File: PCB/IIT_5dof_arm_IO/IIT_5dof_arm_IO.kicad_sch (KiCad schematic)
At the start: 69 parts, among them J1 Conn_02x13_Top_Bottom, J10 Conn_01x06, J11 Conn_01x06, J12 Conn_01x04, J13 Conn_01x04, J2 Conn_01x06, J3 Conn_01x06, J4 Conn_01x06, J5 Conn_01x05, J6 Conn_01x03, J7 Conn_02x03_Counter_Clockwise, J8 Conn_01x03, J9 Conn_01x06, SW1 SW_Push, SW10 SW_Push, SW11 SW_Push, SW12 SW_Push, SW13 SW_Push, SW14 SW_Push, SW2 SW_Push, SW3 SW_Push, SW4 SW_Push, SW5 SW_Push, SW6 SW_Push, SW7 RotaryEncoder_Switch, SW8 SW_Push, SW9 SW_Push, U1 ATmega328P-A, Y1 16MHz

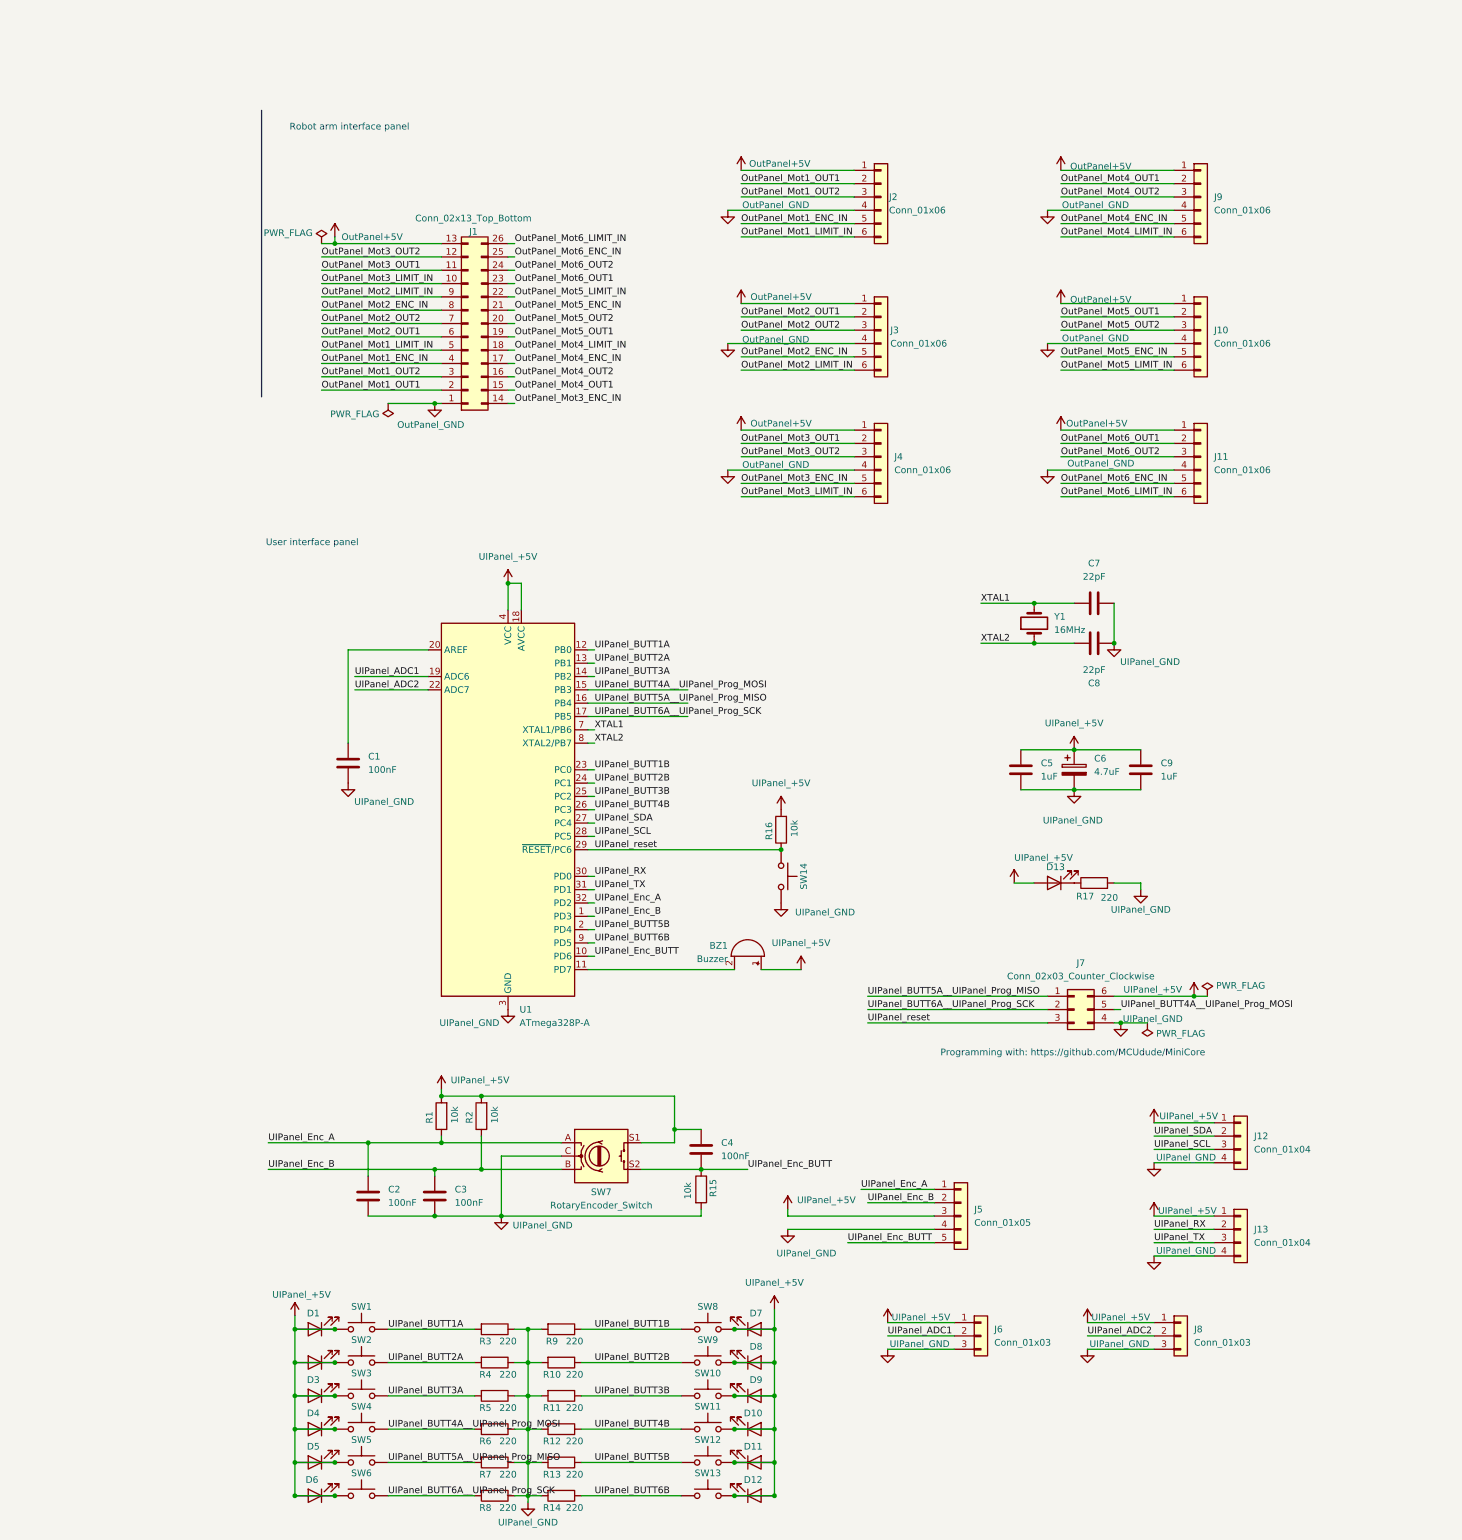
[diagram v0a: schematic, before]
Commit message: Split control board and I/O cards into separate projects
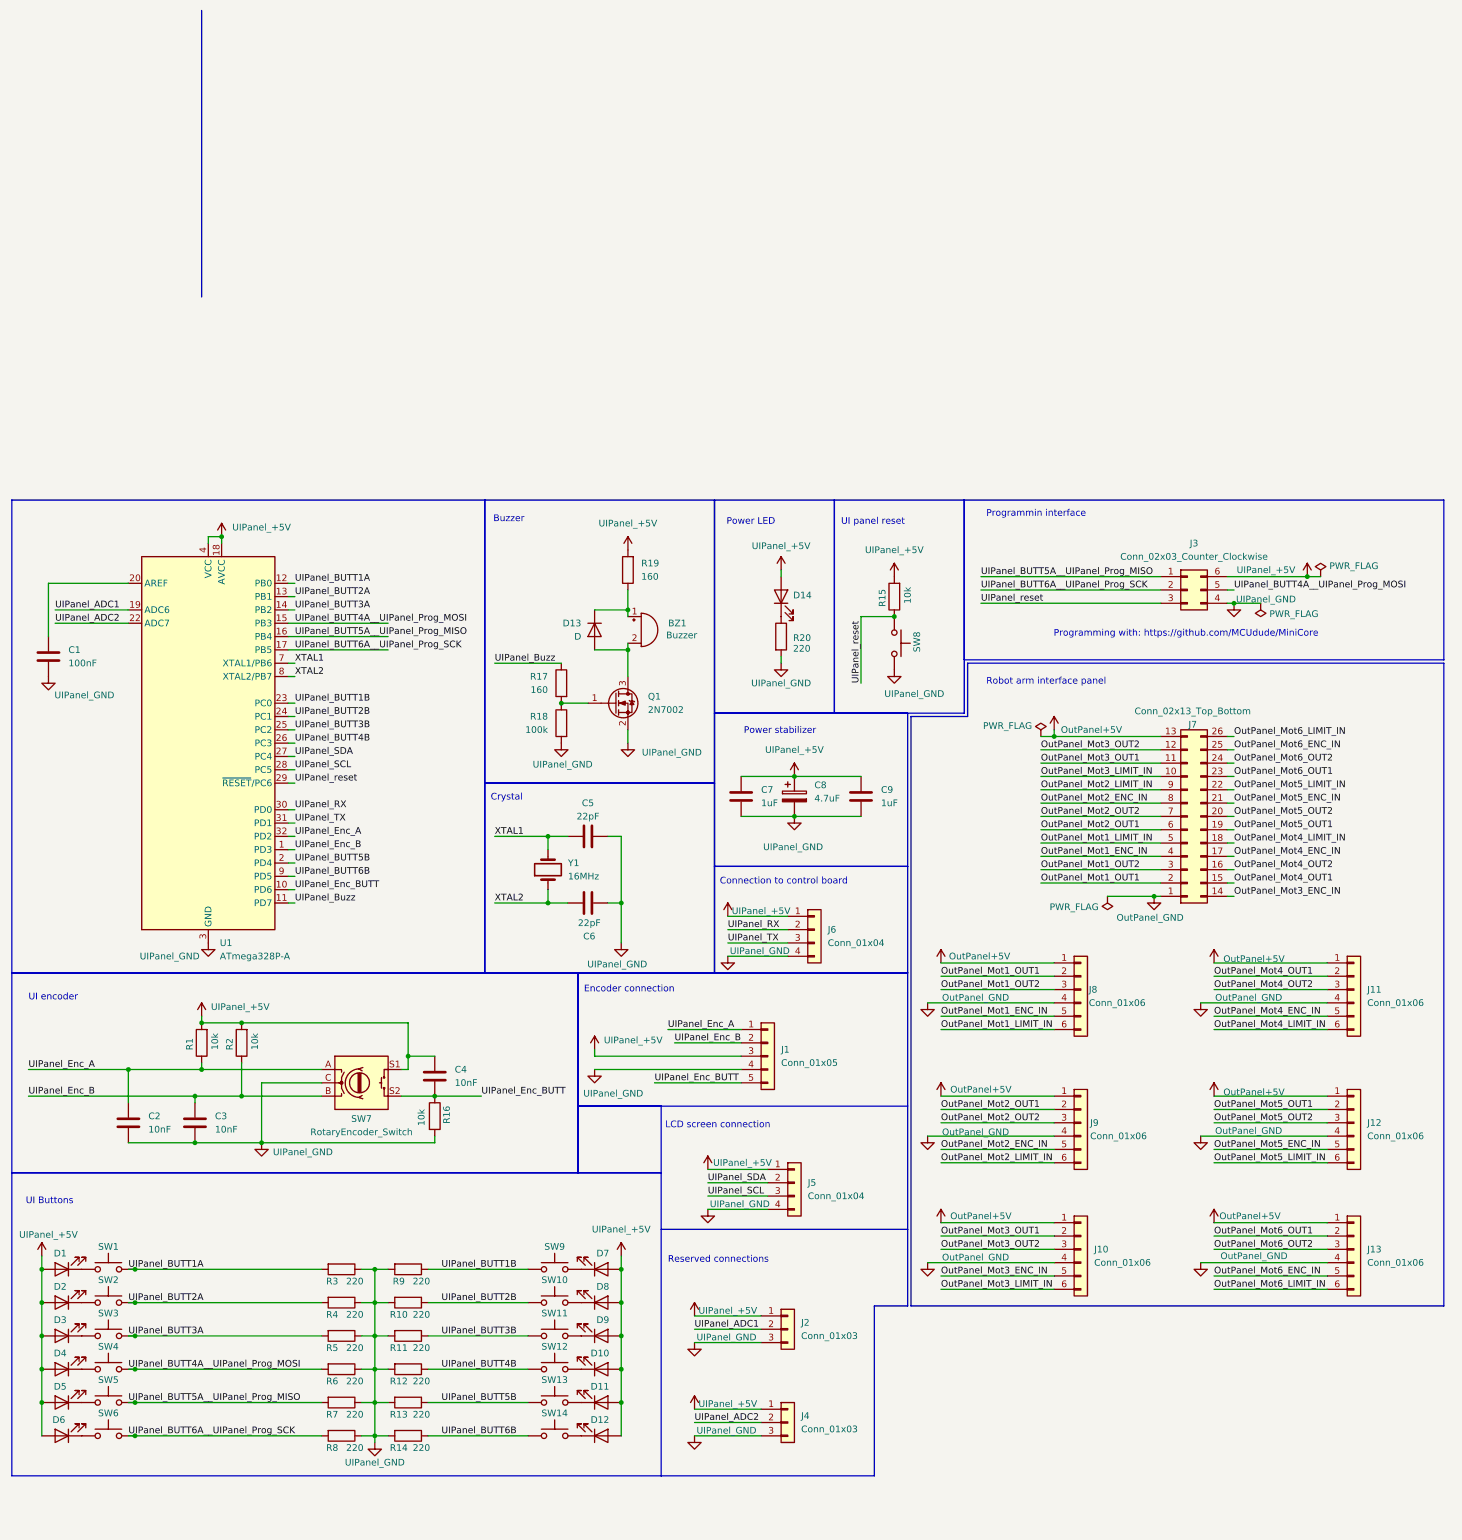
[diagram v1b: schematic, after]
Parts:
- removed C6: 4.7uF, Capacitor_SMD:C_1206_3216Metric_Pad1.33x1.80mm_HandSolder, symbol Device:C_Polarized
- removed C8: 22pF, Capacitor_SMD:C_0805_2012Metric_Pad1.18x1.45mm_HandSolder, symbol Device:C
- removed D13: LED, LED_THT:LED_D5.0mm, symbol Device:LED
- removed J1: Conn_02x13_Top_Bottom, Connector_IDC:IDC-Header_2x13_P2.54mm_Vertical, symbol Connector_Generic:Conn_02x13_Top_Bottom
- removed J12, J13: Conn_01x04, Connector_Molex:Molex_KK-254_AE-6410-04A_1x04_P2.54mm_Vertical, symbol Connector_Generic:Conn_01x04
- removed J2, J3, J4: Conn_01x06, Connector_Molex:Molex_KK-254_AE-6410-06A_1x06_P2.54mm_Vertical, symbol Connector_Generic:Conn_01x06
- removed J5: Conn_01x05, Connector_Molex:Molex_KK-254_AE-6410-05A_1x05_P2.54mm_Vertical, symbol Connector_Generic:Conn_01x05
- removed J6, J8: Conn_01x03, Connector_Molex:Molex_KK-254_AE-6410-03A_1x03_P2.54mm_Vertical, symbol Connector_Generic:Conn_01x03
- removed J7: Conn_02x03_Counter_Clockwise, Connector_PinHeader_2.54mm:PinHeader_2x03_P2.54mm_Vertical, symbol Connector_Generic:Conn_02x03_Counter_Clockwise
- added C6: 22pF, Capacitor_SMD:C_0805_2012Metric_Pad1.18x1.45mm_HandSolder, symbol Device:C
- added C8: 4.7uF, Capacitor_SMD:C_1206_3216Metric_Pad1.33x1.80mm_HandSolder, symbol Device:C_Polarized
- added D13: D, symbol Device:D
- added D14: LED, LED_THT:LED_D5.0mm, symbol Device:LED
- added J1: Conn_01x05, Connector_Molex:Molex_KK-254_AE-6410-05A_1x05_P2.54mm_Vertical, symbol Connector_Generic:Conn_01x05
- added J12, J13, J8: Conn_01x06, Connector_Molex:Molex_KK-254_AE-6410-06A_1x06_P2.54mm_Vertical, symbol Connector_Generic:Conn_01x06
- added J2, J4: Conn_01x03, Connector_Molex:Molex_KK-254_AE-6410-03A_1x03_P2.54mm_Vertical, symbol Connector_Generic:Conn_01x03
- added J3: Conn_02x03_Counter_Clockwise, Connector_PinHeader_2.54mm:PinHeader_2x03_P2.54mm_Vertical, symbol Connector_Generic:Conn_02x03_Counter_Clockwise
- added J5, J6: Conn_01x04, Connector_Molex:Molex_KK-254_AE-6410-04A_1x04_P2.54mm_Vertical, symbol Connector_Generic:Conn_01x04
- added J7: Conn_02x13_Top_Bottom, Connector_IDC:IDC-Header_2x13_P2.54mm_Vertical, symbol Connector_Generic:Conn_02x13_Top_Bottom
- added Q1: 2N7002, Package_TO_SOT_SMD:SOT-23, symbol Transistor_FET:2N7002
- added R18: 100k, symbol Device:R
- added R19: 160, symbol Device:R
- added R20: 220, Resistor_SMD:R_0805_2012Metric_Pad1.20x1.40mm_HandSolder, symbol Device:R
- C2, C3, C4: value 100nF -> 10nF
- C5: value 1uF -> 22pF
- C7: value 22pF -> 1uF
- R17: value 220 -> 160; footprint Resistor_SMD:R_0805_2012Metric_Pad1.20x1.40mm_HandSolder -> (none)
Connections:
- net OutPanel+5V: now also J12.1 (Pin_1), J13.1 (Pin_1), J7.13 (Pin_13), J8.1 (Pin_1)
- net OutPanel_GND: now also J12.4 (Pin_4), J13.4 (Pin_4), J7.1 (Pin_1), J8.4 (Pin_4)
- net OutPanel_Mot1_ENC_IN: now also J7.4 (Pin_4), J8.5 (Pin_5)
- net OutPanel_Mot1_LIMIT_IN: now also J7.5 (Pin_5), J8.6 (Pin_6)
- net OutPanel_Mot1_OUT1: now also J7.2 (Pin_2), J8.2 (Pin_2)
- net OutPanel_Mot1_OUT2: now also J7.3 (Pin_3), J8.3 (Pin_3)
- net OutPanel_Mot2_ENC_IN: now also J9.5 (Pin_5), J7.8 (Pin_8)
- net OutPanel_Mot2_LIMIT_IN: now also J9.6 (Pin_6), J7.9 (Pin_9)
- net OutPanel_Mot2_OUT1: now also J9.2 (Pin_2), J7.6 (Pin_6)
- net OutPanel_Mot2_OUT2: now also J9.3 (Pin_3), J7.7 (Pin_7)
- net OutPanel_Mot3_ENC_IN: now also J10.5 (Pin_5), J7.14 (Pin_14)
- net OutPanel_Mot3_LIMIT_IN: now also J10.6 (Pin_6), J7.10 (Pin_10)
- net OutPanel_Mot3_OUT1: now also J10.2 (Pin_2), J7.11 (Pin_11)
- net OutPanel_Mot3_OUT2: now also J10.3 (Pin_3), J7.12 (Pin_12)
- net OutPanel_Mot4_ENC_IN: now also J11.5 (Pin_5), J7.17 (Pin_17); no longer J9.5 (Pin_5)
- net OutPanel_Mot4_LIMIT_IN: now also J11.6 (Pin_6), J7.18 (Pin_18); no longer J9.6 (Pin_6)
- net OutPanel_Mot4_OUT1: now also J11.2 (Pin_2), J7.15 (Pin_15); no longer J9.2 (Pin_2)
- net OutPanel_Mot4_OUT2: now also J11.3 (Pin_3), J7.16 (Pin_16); no longer J9.3 (Pin_3)
- net OutPanel_Mot5_ENC_IN: now also J12.5 (Pin_5), J7.21 (Pin_21); no longer J10.5 (Pin_5)
- net OutPanel_Mot5_LIMIT_IN: now also J12.6 (Pin_6), J7.22 (Pin_22); no longer J10.6 (Pin_6)
- net OutPanel_Mot5_OUT1: now also J12.2 (Pin_2), J7.19 (Pin_19); no longer J10.2 (Pin_2)
- net OutPanel_Mot5_OUT2: now also J12.3 (Pin_3), J7.20 (Pin_20); no longer J10.3 (Pin_3)
- net OutPanel_Mot6_ENC_IN: now also J13.5 (Pin_5), J7.25 (Pin_25); no longer J11.5 (Pin_5)
- net OutPanel_Mot6_LIMIT_IN: now also J13.6 (Pin_6), J7.26 (Pin_26); no longer J11.6 (Pin_6)
- net OutPanel_Mot6_OUT1: now also J13.2 (Pin_2), J7.23 (Pin_23); no longer J11.2 (Pin_2)
- net OutPanel_Mot6_OUT2: now also J13.3 (Pin_3), J7.24 (Pin_24); no longer J11.3 (Pin_3)
- net UIPanel_+5V: now also C7.1, R15.2, C8.1, D14.2 (A), J1.3 (Pin_3), J2.1 (Pin_1), J3.6 (Pin_6), J4.1 (Pin_1), J5.1 (Pin_1), J6.1 (Pin_1), R19.2; no longer BZ1.1 (+), C5.1, D1.1 (K), D10.1 (K), D11.1 (K), D12.1 (K), D2.1 (K), D3.1 (K), D4.1 (K), D5.1 (K), D6.1 (K), D7.1 (K), D8.1 (K), D9.1 (K), R16.2, SW1.1, SW10.1, SW11.1, SW12.1, SW13.1, SW2.1, SW3.1, SW4.1, SW5.1, SW6.1, SW8.1, SW9.1
- net UIPanel_ADC1: now also J2.2 (Pin_2)
- net UIPanel_ADC2: now also J4.2 (Pin_2)
- net UIPanel_BUTT1B: now also SW9.2; no longer SW8.2
- net UIPanel_BUTT2B: now also SW10.2; no longer SW9.2
- net UIPanel_BUTT3B: now also SW11.2; no longer SW10.2
- net UIPanel_BUTT4A__UIPanel_Prog_MOSI: now also J3.5 (Pin_5)
- net UIPanel_BUTT4B: now also SW12.2; no longer SW11.2
- net UIPanel_BUTT5A__UIPanel_Prog_MISO: now also J3.1 (Pin_1)
- net UIPanel_BUTT5B: now also SW13.2; no longer SW12.2
- net UIPanel_BUTT6A__UIPanel_Prog_SCK: now also J3.2 (Pin_2)
- net UIPanel_BUTT6B: now also SW14.2; no longer SW13.2
- net UIPanel_Enc_A: now also J1.1 (Pin_1)
- net UIPanel_Enc_B: now also J1.2 (Pin_2)
- net UIPanel_Enc_BUTT: now also R16.1, J1.5 (Pin_5); no longer R15.1
- net UIPanel_GND: now also R16.2, SW8.2, C6.1, C8.2, J1.4 (Pin_4), J2.3 (Pin_3), J3.4 (Pin_4), J4.3 (Pin_3), J5.4 (Pin_4), J6.4 (Pin_4), Q1.2 (S), R18.2, R20.2; no longer R15.2, R17.2, SW14.2
- net UIPanel_RX: now also J6.2 (Pin_2)
- net UIPanel_SCL: now also J5.3 (Pin_3)
- net UIPanel_SDA: now also J5.2 (Pin_2)
- net UIPanel_TX: now also J6.3 (Pin_3)
- net UIPanel_reset: now also R15.1, SW8.1, J3.3 (Pin_3); no longer R16.1, SW14.1
- net XTAL1: now also C5.1; no longer C7.1
- net XTAL2: now also C6.2
- net UIPanel_Buzz: now reaches R17.1
- net UIPanel_Buzz: now also U1.11 (PD7)
- net at BZ1.2 (-): now also D13.2 (A), Q1.3 (D); no longer U1.11 (PD7)
- new net: D2.1 (K), SW2.1
- new net: D6.1 (K), SW6.1
- new net: D3.1 (K), SW3.1
- new net: BZ1.1 (+), D13.1 (K), R19.1
- new net: D12.1 (K), SW14.1
- new net: D7.1 (K), SW9.1
- new net: Q1.1 (G), R17.2, R18.1
- new net: D5.1 (K), SW5.1
- new net: D10.1 (K), SW12.1
- new net: D14.1 (K), R20.1
- new net: D8.1 (K), SW10.1
- new net: D4.1 (K), SW4.1
- new net: D11.1 (K), SW13.1
- new net: D1.1 (K), SW1.1
- new net: D9.1 (K), SW11.1
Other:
- note added: "Buzzer"
- note added: "Connection to control board"
- note added: "Crystal"
- note added: "Encoder connection"
- note added: "LCD screen connection"
- note added: "Power LED"
- note added: "Power stabilizer"
- note added: "Programmin interface"
- note added: "Reserved connections"
- note added: "UI Buttons"
- note added: "UI encoder"
- note added: "UI panel reset"
- note removed: "User interface panel"
- title: (none) -> IIT 5dof Robot arm I/O panels

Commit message: Organize schematic and generate initi PCB
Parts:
- D13: footprint (none) -> Diode_SMD:D_0805_2012Metric_Pad1.15x1.40mm_HandSolder
- D14: footprint LED_THT:LED_D5.0mm -> Connector_Molex:Molex_KK-254_AE-6410-02A_1x02_P2.54mm_Vertical
- R17, R18, R19: footprint (none) -> Resistor_SMD:R_0805_2012Metric_Pad1.20x1.40mm_HandSolder
- SW8: footprint Connector_Molex:Molex_KK-254_AE-6410-02A_1x02_P2.54mm_Vertical -> Button_Switch_SMD:SW_SPST_FSMSM
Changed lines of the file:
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@@
 			)
 		)
-		(property "Footprint" ""
+		(property "Footprint" "Resistor_SMD:R_0805_2012Metric_Pad1.20x1.40mm_HandSolder"
 			(at 118.618 46.99 90)
 			(effects
@@
 		(exclude_from_sim no)
 		(in_bom yes)
-		(on_board no)
+		(on_board yes)
 		(dnp no)
 		(property "Reference" "SW8"
@@
 			)
 		)
-		(property "Footprint" "Connector_Molex:Molex_KK-254_AE-6410-02A_1x02_P2.54mm_Vertical"
+		(property "Footprint" "Button_Switch_SMD:SW_SPST_FSMSM"
 			(at 185.42 39.37 0)
 			(effects
@@
 			)
 		)
-		(property "Footprint" ""
+		(property "Footprint" "Resistor_SMD:R_0805_2012Metric_Pad1.20x1.40mm_HandSolder"
 			(at 118.618 54.61 90)
 			(effects
@@
 			)
 		)
-		(property "Footprint" ""
+		(property "Footprint" "Resistor_SMD:R_0805_2012Metric_Pad1.20x1.40mm_HandSolder"
 			(at 131.318 25.4 90)
 			(effects
@@
 			)
 		)
-		(property "Footprint" ""
+		(property "Footprint" "Diode_SMD:D_0805_2012Metric_Pad1.15x1.40mm_HandSolder"
 			(at 123.19 36.83 0)
 			(effects
@@
 			)
 		)
-		(property "Footprint" "LED_THT:LED_D5.0mm"
+		(property "Footprint" "Connector_Molex:Molex_KK-254_AE-6410-02A_1x02_P2.54mm_Vertical"
 			(at 158.75 30.48 0)
 			(effects
